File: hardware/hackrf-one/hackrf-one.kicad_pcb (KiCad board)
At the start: 4 copper layers, 120 x 75 mm, 431 parts, among them J1 USB-MICRO-B, J10 GND_CLIP, J2 RF-SHIELD-FRAME, J3 RF-SHIELD-COVER, J4 MOUNTING_HOLE, J5 MOUNTING_HOLE, J6 MOUNTING_HOLE, J7 MOUNTING_HOLE, J8 MOUNTING_HOLE, J9 MOUNTING_HOLE, P13 GPO1, P14 XCVR_CLKOUT, P15 INTR, P16 CLKIN, P17 GPO6, P18 OEB, P19 GPO3, P2 CLKOUT, P20 GPIO, P21 REF_IN, P22 I2S, P23 DBGEN, P24 TRST, P25 LPC_ISP, P26 LPC_JTAG, P27 MIXER_SDATA, P28 SD, P29 CPLD_JTAG, P3 GND, P30 BANK2_AUX, P31 MIXER_SCLK, P32 MIXER_ENX, P33 MIXER_RESETX, P34 MIX_BYPASS, P35 !MIX_BYPASS, P37 SCL, P38 SDA, P39 SSP1_SCK, P4 ANTENNA, P40 SSP1_COPI, P41 SSP1_CIPO, P43 RX, P44 HP, P45 LP, P46 TX_MIX_BP, P47 RX_MIX_BP, P48 TX_AMP, P49 RX_AMP, P5 LEDS, P50 AMP_BYPASS, P51 !TX_AMP_PWR, P52 !RX_AMP_PWR, P53 CS_XCVR, P54 CS_AD, P55 TXENABLE, P56 RXENABLE, P57 XTAL2, P58 GCK1, P59 GCK2, P6 GPO4, P60 SGPIO_CLK, P61 DA0, P62 DA7, P63 DD0, P64 DD9, P65 DA4, P66 DD5, P67 RSSI, P68 SPIFI_CS, P69 VREGMODE, P7 GPO2, P70 EN_1V8, P71 ID, P72 GP_CLKIN, P73 P1_2, P74 P1_1, P75 GP_CLKIN, P76 GP_CLKIN, P77 GP_CLKIN, P78 GP_CLKIN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

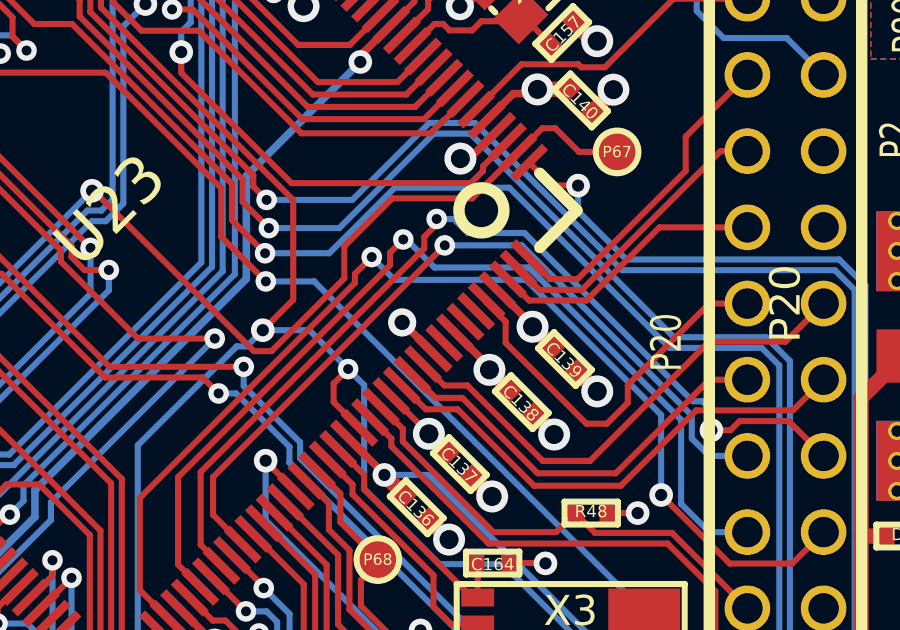
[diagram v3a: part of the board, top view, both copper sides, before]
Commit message: HackRF One: add ADC pin straps for hardware version detection
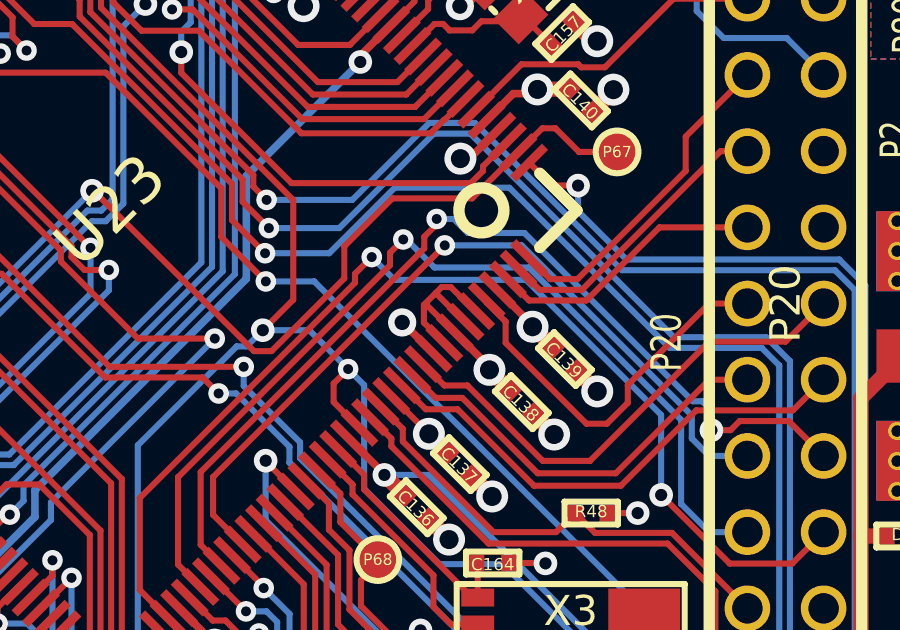
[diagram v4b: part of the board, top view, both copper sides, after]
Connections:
- U23 pad 136: (no net) -> VCC
- U23 pad 138: (no net) -> VCC
- U23 pad 139: (no net) -> VCC
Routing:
- net VCC: track 181.1 -> 187.8 mm
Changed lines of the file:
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@@
     (thickness 1.6002)
     (drawings 177)
-    (tracks 4377)
+    (tracks 4389)
     (zones 0)
     (modules 431)
@@
     (0 C1F signal)
     (1 C2 signal)
-    (2 C3 signal hide)
+    (2 C3 signal)
     (31 C4B signal)
     (32 B.Adhes user)
@@
     (34 B.Paste user)
     (35 F.Paste user)
-    (36 B.SilkS user)
+    (36 B.SilkS user hide)
     (37 F.SilkS user)
     (38 B.Mask user)
-    (39 F.Mask user)
+    (39 F.Mask user hide)
     (41 Cmts.User user)
     (44 Edge.Cuts user)
@@
       (net 192 GND) (die_length -1518.485687))
     (pad 136 smd rect (at -4.7498 -11.00074 315) (size 1.50114 0.29464) (layers C1F F.Paste F.Mask)
-      (die_length -1518.485687))
+      (net 219 VCC) (die_length -1518.485687))
     (pad 137 smd rect (at -5.25018 -11.00074 315) (size 1.50114 0.29464) (layers C1F F.Paste F.Mask)
       (net 219 VCC) (die_length 0.12192))
     (pad 138 smd rect (at -5.75056 -11.00074 315) (size 1.50114 0.29464) (layers C1F F.Paste F.Mask)
-      (die_length 0.01524))
+      (net 219 VCC) (die_length 0.01524))
     (pad 139 smd rect (at -6.25094 -11.00074 315) (size 1.50114 0.29464) (layers C1F F.Paste F.Mask)
-      (die_length -1518.485687))
+      (net 219 VCC) (die_length -1518.485687))
     (pad 140 smd rect (at -6.74878 -11.00074 315) (size 1.50114 0.29464) (layers C1F F.Paste F.Mask)
       (net 93 /mcu/usb/power/GPIO3_15) (die_length -1518.485687))
@@
   (segment (start 163.328836 143.973451) (end 163.328836 144.023741) (width 0.254) (layer C1F) (net 219))
   (segment (start 164.029296 144.724201) (end 163.328836 144.023741) (width 0.508) (layer C1F) (net 219) (status 10))
+  (segment (start 159.706293 143.885537) (end 160.385108 144.564352) (width 0.2032) (layer C1F) (net 219))
+  (segment (start 159.706293 143.885537) (end 159.706293 143.293707) (width 0.2032) (layer C1F) (net 219))
+  (segment (start 161.092752 143.856708) (end 161.056708 143.856708) (width 0.2032) (layer C1F) (net 219))
+  (segment (start 161.056708 143.856708) (end 160.1 142.9) (width 0.2032) (layer C1F) (net 219))
+  (segment (start 159.706293 143.293707) (end 160.1 142.9) (width 0.2032) (layer C1F) (net 219))
+  (segment (start 160.73893 144.21053) (end 160.71053 144.21053) (width 0.2032) (layer C1F) (net 219))
+  (segment (start 159.793707 143.293707) (end 159.706293 143.293707) (width 0.2032) (layer C1F) (net 219))
+  (segment (start 160.71053 144.21053) (end 159.793707 143.293707) (width 0.2032) (layer C1F) (net 219))
+  (segment (start 160.6 142.7) (end 160.3 142.7) (width 0.2032) (layer C1F) (net 219) (status 1000000))
+  (segment (start 161.402886 143.502886) (end 160.6 142.7) (width 0.2032) (layer C1F) (net 219) (status 1000000))
+  (segment (start 161.446574 143.502886) (end 161.402886 143.502886) (width 0.2032) (layer C1F) (net 219) (status 1000000))
+  (segment (start 160.1 142.9) (end 160.3 142.7) (width 0.2032) (layer C1F) (net 219))
   (via (at 142.7024 127.8576) (size 0.7874) (drill 0.4064) (layers C1F C4B) (net 220))
   (segment (start 142.7024 127.8576) (end 141.0768 126.232) (width 0.2032) (layer C1F) (net 220))

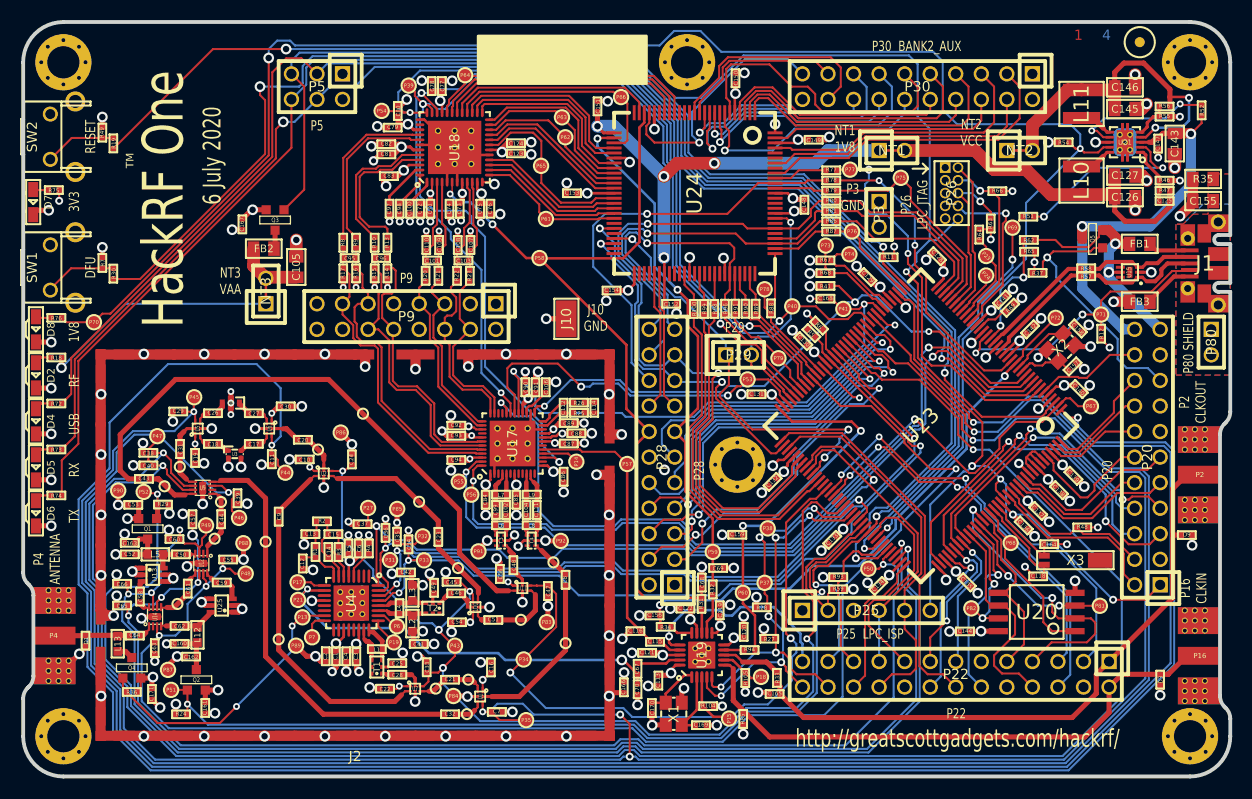
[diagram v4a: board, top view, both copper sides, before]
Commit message: HackRF One: update silkscreen
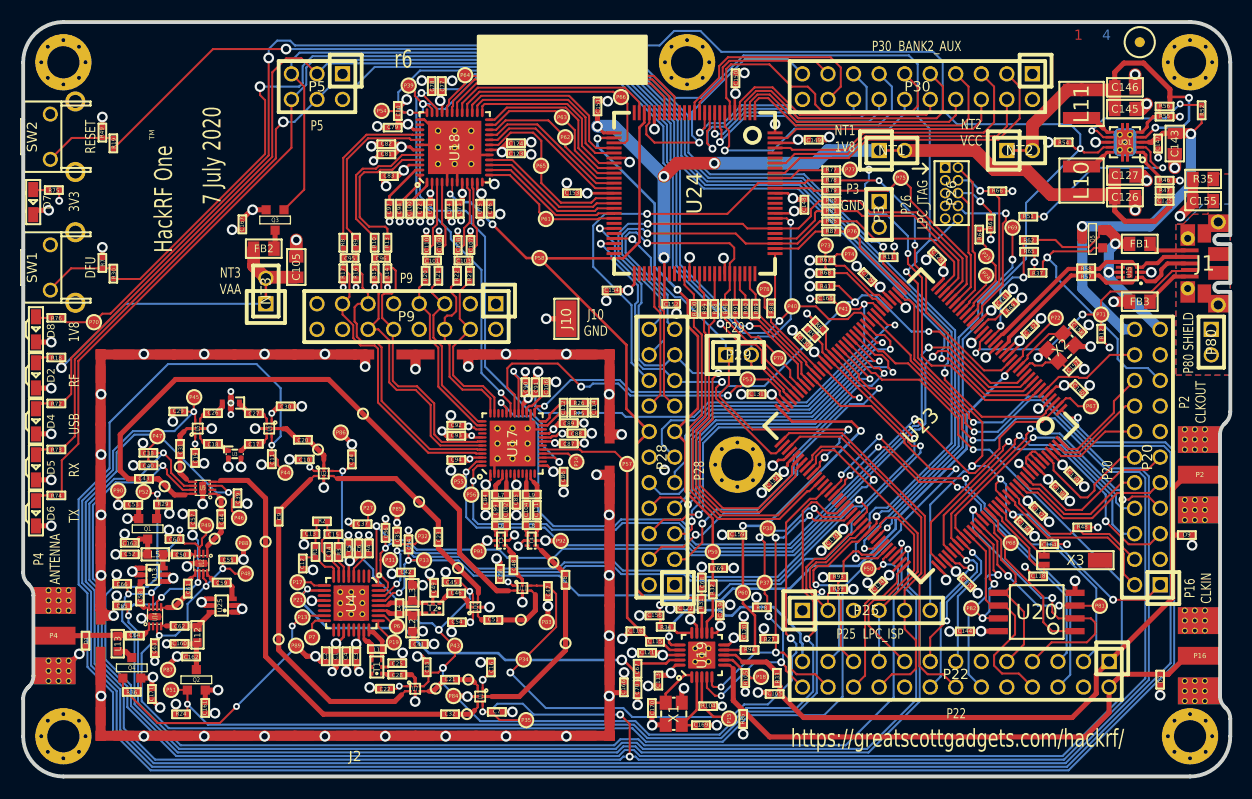
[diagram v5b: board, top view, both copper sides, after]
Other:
- board text added: "7 July 2020"
- board text added: "https://greatscottgadgets.com/hackrf/"
- board text added: "r6"
- board text removed: "6 July 2020"
- board text removed: "http://greatscottgadgets.com/hackrf/"
